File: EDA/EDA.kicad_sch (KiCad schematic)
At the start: 38 parts, among them J2 Screw_Terminal_01x02, M1 Motor_Servo, U1 PMCF8316A1VRGFR, U2 LM2596S-5, U3 LM2678S-5

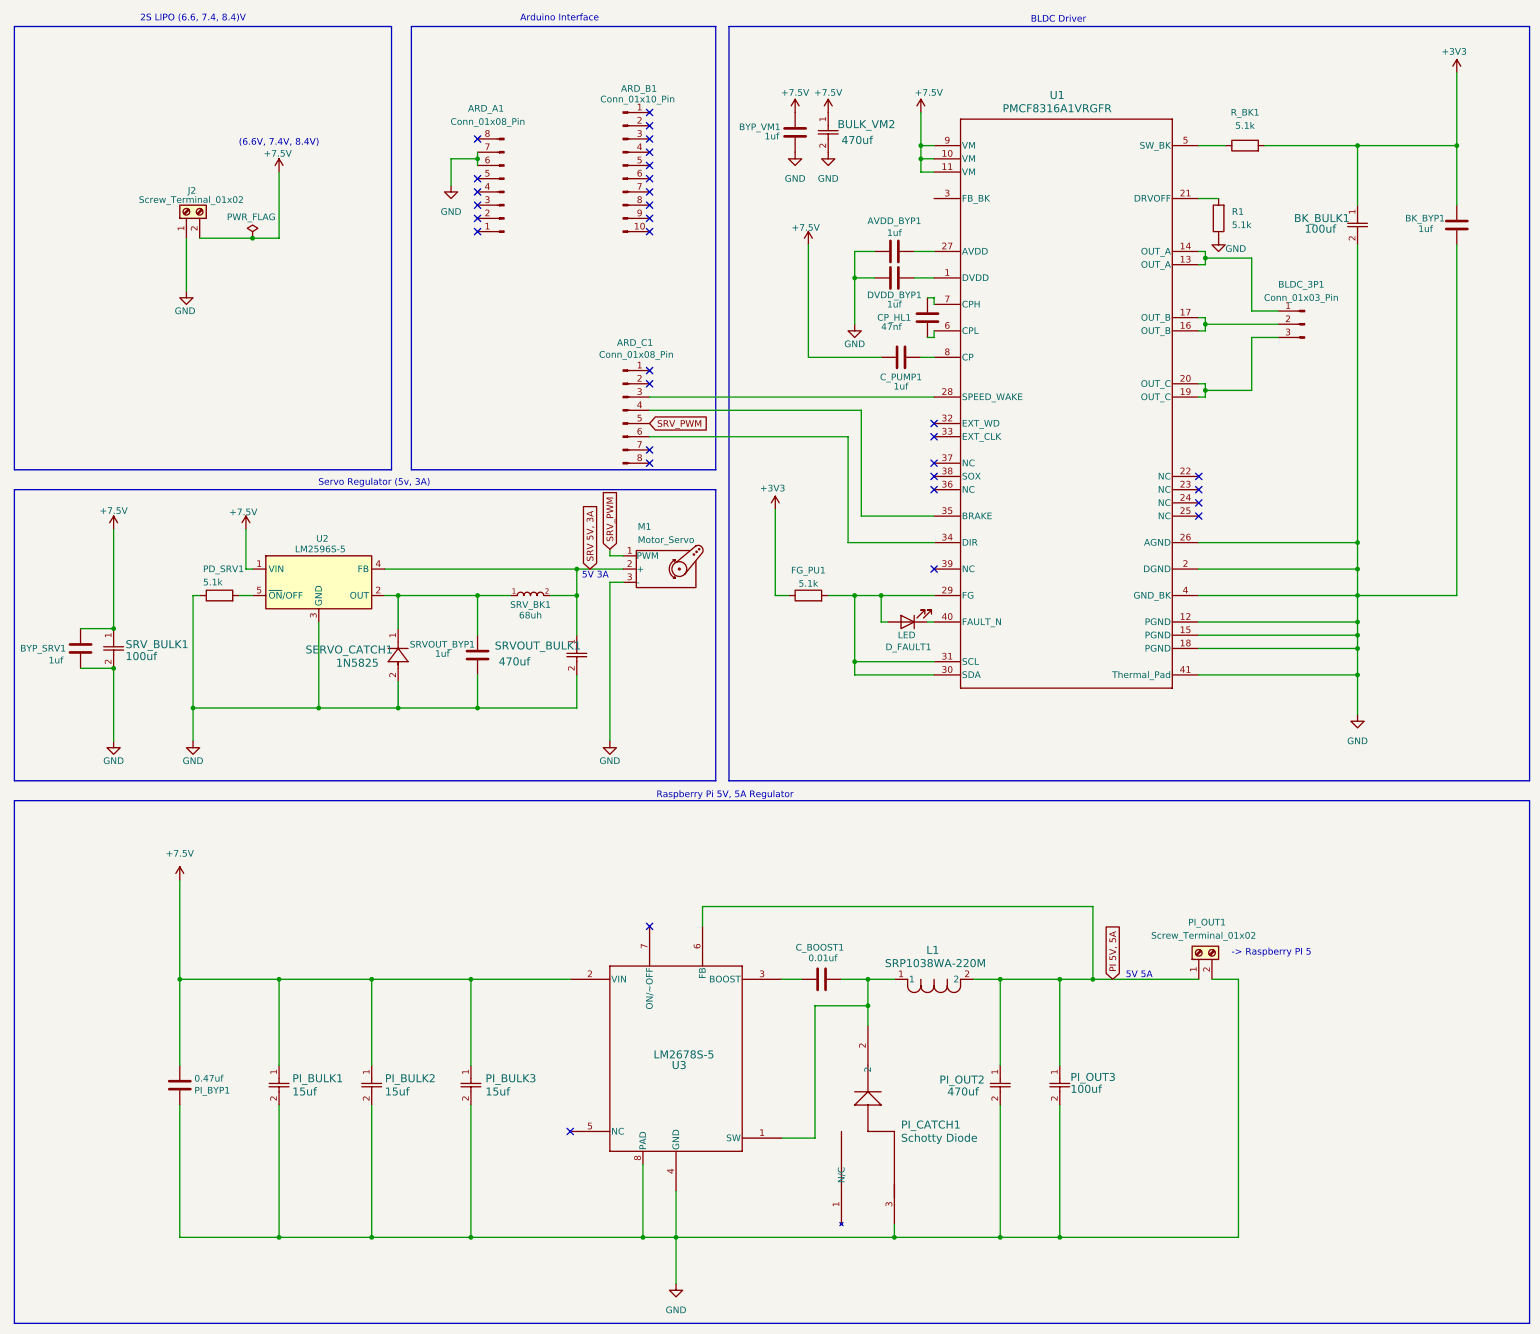
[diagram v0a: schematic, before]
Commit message: Add LM2678S-12 symbol and footprints to KiCAD library
- Created a new symbol for the LM2678S-12 in the KiCAD symbol library.
- Added three footprints (TS7B, TS7B-L, TS7B-M) for the LM2678S-12 in the KiCAD footprint library.
- Each footprint includes detailed pad and line definitions, along with silk screen and courtyard outlines.
- Updated properties for reference, value, and datasheet links in the symbol and footprints.
- Refactor schematic for clarity and readablity.
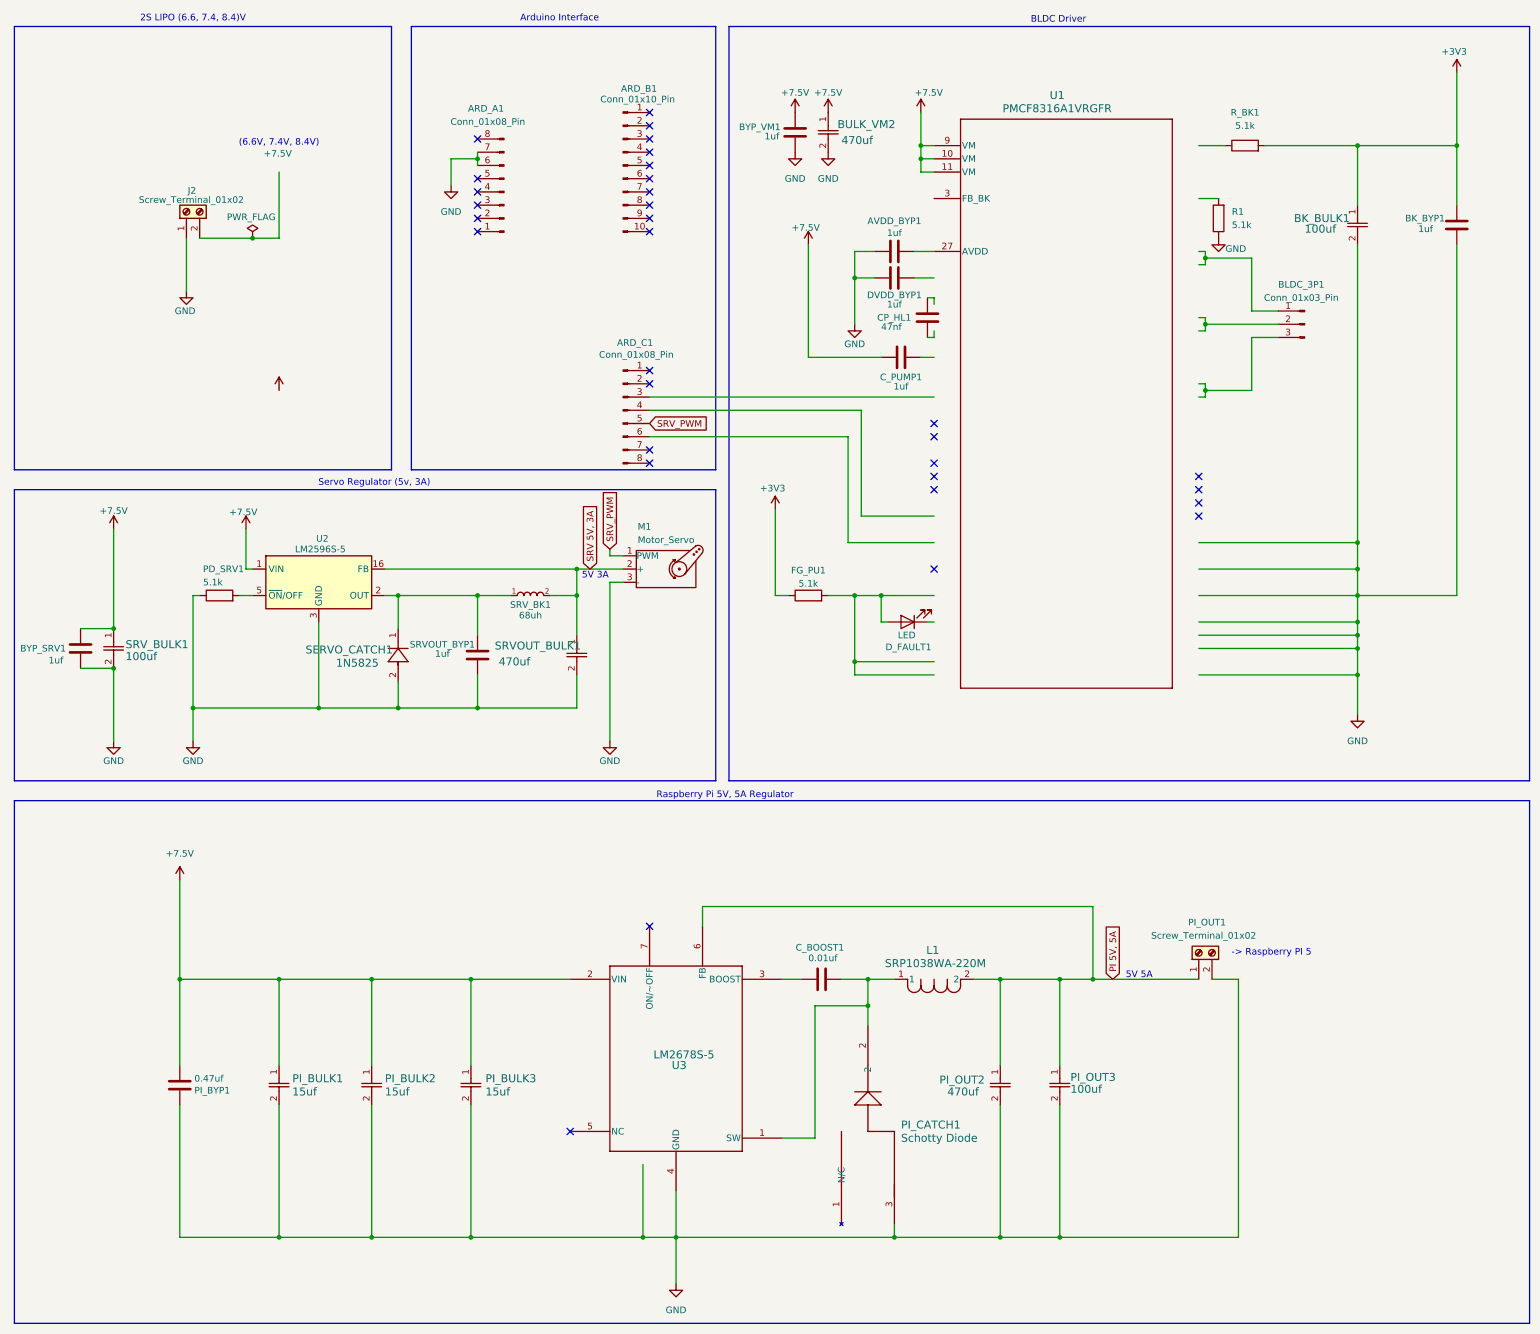
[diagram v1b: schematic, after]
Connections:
- net +7.5V: no longer J2.2 (Pin_2)
- net GND: no longer U1.12 (PGND), U1.15 (PGND), U1.18 (PGND), U1.2 (DGND), U1.26 (AGND), U1.4 (GND_BK), U1.41 (Thermal_Pad), U3.8 (PAD)
- net SRV 5V, 3A: now also U2.16 (FB); no longer U2.4 (FB)
- net at R_BK1.1: no longer U1.5 (SW_BK)
- net at ARD_C1.3 (Pin_3): no longer U1.28 (SPEED_WAKE)
- net at ARD_C1.4 (Pin_4): no longer U1.35 (BRAKE)
- net at ARD_C1.6 (Pin_6): no longer U1.34 (DIR)
- net at DVDD_BYP1.1: no longer U1.1 (DVDD)
- net at R1.2: no longer U1.21 (DRVOFF)
- net at D_FAULT1.1 (K): no longer U1.40 (FAULT_N)
- net at CP_HL1.2: no longer U1.6 (CPL)
- net at CP_HL1.1: no longer U1.7 (CPH)
- net at C_PUMP1.2: no longer U1.8 (CP)
- new net: D_FAULT1.2 (A), FG_PU1.2
- now unconnected: BLDC_3P1.1 (Pin_1), BLDC_3P1.2 (Pin_2), BLDC_3P1.3 (Pin_3)
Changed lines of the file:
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@@
 	(symbol
 		(lib_id "power:+7.5V")
-		(at 67.31 44.45 0)
+		(at 67.31 86.36 0)
 		(unit 1)
 		(exclude_from_sim no)
@@
 		(dnp no)
 		(property "Reference" "#PWR01"
-			(at 67.31 48.26 0)
+			(at 67.31 90.17 0)
 			(effects
 				(font
@@
 		)
 		(property "Footprint" ""
-			(at 67.31 44.45 0)
+			(at 67.31 86.36 0)
 			(effects
 				(font
@@
 		)
 		(property "Datasheet" ""
-			(at 67.31 44.45 0)
+			(at 67.31 86.36 0)
 			(effects
 				(font
@@
 		)
 		(property "Description" "Power symbol creates a global label with name \"+7.5V\""
-			(at 67.31 44.45 0)
+			(at 67.31 86.36 0)
 			(effects
 				(font
@@
 				(font
 					(size 1.27 1.27)
-					(italic yes)
 				)
 				(hide yes)
@@
 			)
 		)
+		(pin "2"
+		)
 		(pin "1"
